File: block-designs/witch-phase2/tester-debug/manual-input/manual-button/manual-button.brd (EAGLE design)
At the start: 27.9 x 27.9 mm, 8 parts

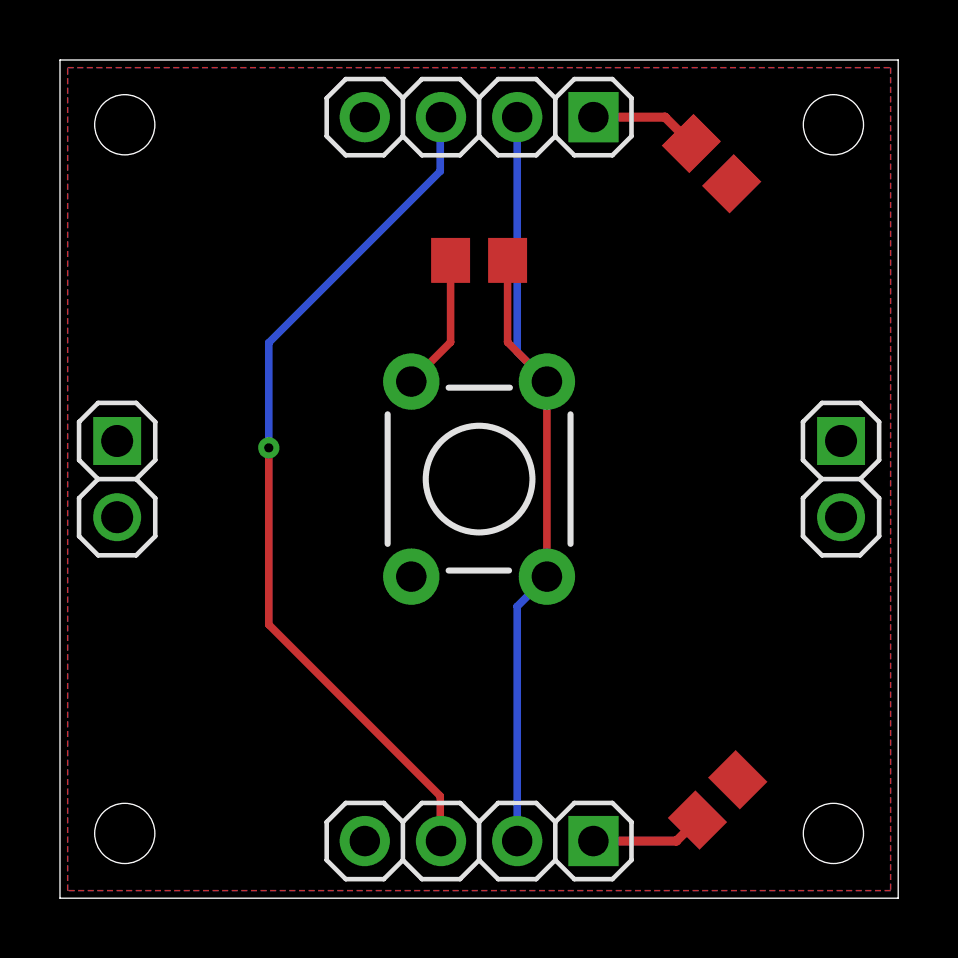
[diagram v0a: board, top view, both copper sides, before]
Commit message: switch to using a schmitt trigger with OR gate for clock output
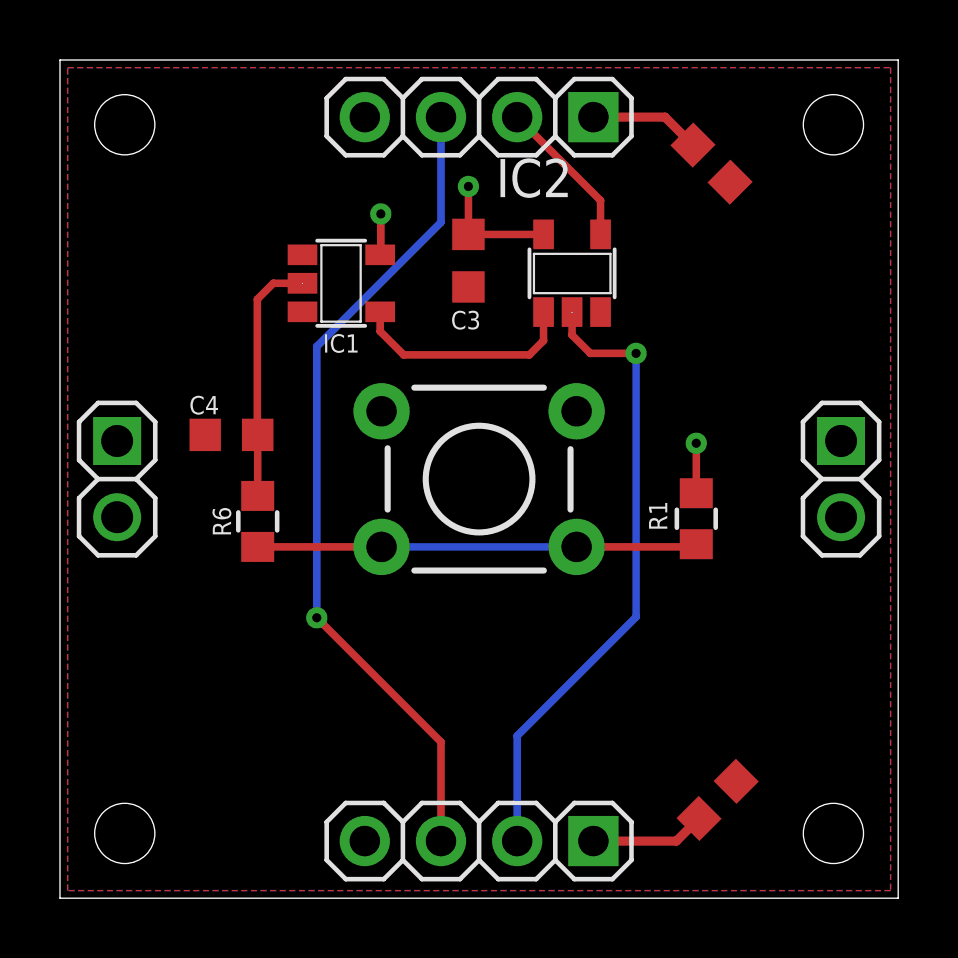
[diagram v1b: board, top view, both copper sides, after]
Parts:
- added C4: 1uF, resistor:C0603K
- added IC1: 74LVC1G14DBV, 74xx-little-us:SOT23-5
- added IC2: 74AHC1G32DBV, 74xx-little-us:SOT23-5
- added R1: 100k, resistor:R0603
- added R6: 10k, resistor:R0603
- C1, C2, C3: device resistor:C0805 -> resistor:C0603K
- moved C3 0.36 mm to (13.6, 21.3), turned to 270 degrees
- turned S1 to 0 degrees
- renumbered S2 to S1
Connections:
- removed net CLOCK: C3.2, JP2.2, JP4.2, S1.1, S1.2
- new net CLOCK_IN: IC2.2, JP4.2
- new net CLOCK_OUT: IC2.4, JP2.2
- new net DA_IN: IC1.4, IC2.1
- new net N$1: R1.1, R6.1, S1.3, S1.4
- new net N$2: C4.1, IC1.2, R6.2
- net GND: now also C3.2, C4.2, IC1.3, IC2.3, S1.1, S1.2
- net VCC: now also IC1.5, IC2.5, R1.2; no longer S1.3, S1.4
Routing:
- net CLOCK: track 29.5 -> 0.00 mm
- net CLOCK_IN: track 0.00 -> 21.1 mm, vias 0 -> 1
- net N$1: track 0.00 -> 14.7 mm
- net N$2: track 0.00 -> 8.28 mm
- net DA_IN: track 0.00 -> 7.58 mm
- net CLOCK_OUT: track 0.00 -> 5.06 mm
- net VCC: track 12.0 -> 14.7 mm, vias 0 -> 3
- net ZC: track 28.8 -> 27.6 mm
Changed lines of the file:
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@@
 </autorouter>
 <elements>
-<element name="C1" library="resistor" package="C0805" value="" x="21.717" y="24.4856" smashed="yes" rot="R315">
+<element name="C1" library="resistor" package="C0603K" value="" x="21.717" y="24.4856" smashed="yes" rot="R315">
 <attribute name="VALUE" x="19.4719375" y="23.49776875" size="1.27" layer="27" rot="R315"/>
 </element>
-<element name="C2" library="resistor" package="C0805" value="" x="21.9202" y="3.2766" smashed="yes" rot="R45">
+<element name="C2" library="resistor" package="C0603K" value="" x="21.9202" y="3.2766" smashed="yes" rot="R45">
 <attribute name="VALUE" x="22.90803125" y="1.031534375" size="1.27" layer="27" rot="R45"/>
 </element>
@@
 <attribute name="VALUE" x="22.86" y="17.78" size="1.27" layer="27" rot="R270"/>
 </element>
-<element name="S2" library="SparkFun-Electromechanical" package="TACTILE-PTH" value="" x="13.97" y="13.97" smashed="yes" rot="R270"/>
-<element name="C3" library="resistor" package="C0805" value="" x="13.97" y="21.2598" smashed="yes">
-<attribute name="VALUE" x="12.7" y="18.7198" size="1.27" layer="27"/>
+<element name="S1" library="SparkFun-Electromechanical" package="TACTILE-PTH" value="" x="13.97" y="13.97" smashed="yes"/>
+<element name="C4" library="resistor" package="C0603K" value="1uF" x="5.715" y="15.4432" smashed="yes" rot="R180">
+<attribute name="NAME" x="5.3086" y="16.7386" size="0.6096" layer="25" rot="R180"/>
+<attribute name="VALUE" x="6.985" y="17.9832" size="1.27" layer="27" rot="R180"/>
 </element>
+<element name="R6" library="resistor" package="R0603" value="10k" x="6.5913" y="12.5603" smashed="yes" rot="R90">
+<attribute name="NAME" x="5.7023" y="12.0523" size="0.6096" layer="25" rot="R90"/>
+<attribute name="VALUE" x="9.1313" y="11.9253" size="1.27" layer="27" rot="R90"/>
+</element>
+<element name="R1" library="resistor" package="R0603" value="100k" x="21.209" y="12.6492" smashed="yes" rot="R90">
+<attribute name="NAME" x="20.2438" y="12.2428" size="0.6096" layer="25" rot="R90"/>
+<attribute name="VALUE" x="23.749" y="12.0142" size="1.27" layer="27" rot="R90"/>
+</element>
+<element name="C3" library="resistor" package="C0603K" value="" x="13.6144" y="21.250909375" smashed="yes" rot="R270">
+<attribute name="NAME" x="13.026490625" y="18.9634" size="0.6096" layer="25"/>
+<attribute name="VALUE" x="11.9644" y="22.050909375" size="1.016" layer="27" rot="R270"/>
+</element>
+<element name="IC1" library="74xx-little-us" package="SOT23-5" value="74LVC1G14DBV" x="9.3726" y="20.4978" smashed="yes" rot="R270">
+<attribute name="NAME" x="8.763" y="18.1864" size="0.6096" layer="25"/>
+<attribute name="VALUE" x="5.5626" y="23.0378" size="1.27" layer="27" rot="R270"/>
+</element>
+<element name="IC2" library="74xx-little-us" package="SOT23-5" value="74AHC1G32DBV" x="17.0688" y="20.828"/>
 </elements>
 <signals>
@@
 <contactref element="JP1" pad="2"/>
 <contactref element="JP3" pad="2"/>
-</signal>
-<signal name="CLOCK">
-<contactref element="JP2" pad="2"/>
-<contactref element="JP4" pad="2"/>
-<contactref element="S2" pad="1"/>
-<contactref element="S2" pad="2"/>
-<wire x1="15.24" y1="26.035" x2="15.24" y2="18.2118" width="0.254" layer="16"/>
-<wire x1="15.24" y1="18.2118" x2="16.2306" y2="17.2212" width="0.254" layer="16"/>
-<wire x1="16.2306" y1="10.7188" x2="15.24" y2="9.7282" width="0.254" layer="16"/>
-<wire x1="15.24" y1="9.7282" x2="15.24" y2="1.905" width="0.254" layer="16"/>
-<wire x1="16.2306" y1="17.2212" x2="16.2306" y2="10.7188" width="0.254" layer="1"/>
+<contactref element="C4" pad="2"/>
+<contactref element="S1" pad="1"/>
+<contactref element="S1" pad="2"/>
 <contactref element="C3" pad="2"/>
-<wire x1="14.92" y1="21.2598" x2="14.92" y2="18.5318" width="0.254" layer="1"/>
-<wire x1="14.92" y1="18.5318" x2="16.2306" y2="17.2212" width="0.254" layer="1"/>
+<contactref element="IC1" pad="3"/>
+<contactref element="IC2" pad="3"/>
 </signal>
 <signal name="ZC">
 <contactref element="JP2" pad="3"/>
 <contactref element="JP4" pad="3"/>
-<via x="6.9596" y="15.0114" extent="1-16" drill="0.3048"/>
-<wire x1="6.9596" y1="15.0114" x2="6.9596" y2="9.1186" width="0.254" layer="1"/>
-<wire x1="6.9596" y1="9.1186" x2="12.6746" y2="3.4036" width="0.254" layer="1"/>
-<wire x1="12.6746" y1="3.4036" x2="12.6746" y2="1.9304" width="0.254" layer="1"/>
-<wire x1="12.6746" y1="1.9304" x2="12.7" y2="1.905" width="0.254" layer="1"/>
-<wire x1="12.6746" y1="26.0096" x2="12.6746" y2="24.2316" width="0.254" layer="16"/>
-<wire x1="12.6746" y1="24.2316" x2="6.9596" y2="18.5166" width="0.254" layer="16"/>
-<wire x1="6.9596" y1="18.5166" x2="6.9596" y2="15.0114" width="0.254" layer="16"/>
-<wire x1="12.6746" y1="26.0096" x2="12.7" y2="26.035" width="0" layer="19" extent="16-16"/>
+<wire x1="12.7" y1="26.035" x2="12.7" y2="22.5298" width="0.254" layer="16"/>
+<via x="8.5598" y="9.3472" extent="1-16" drill="0.3048"/>
+<wire x1="12.7" y1="22.5298" x2="8.5598" y2="18.3896" width="0.254" layer="16"/>
+<wire x1="8.5598" y1="18.3896" x2="8.5598" y2="9.3472" width="0.254" layer="16"/>
+<wire x1="8.5598" y1="9.3472" x2="12.7" y2="5.207" width="0.254" layer="1"/>
+<wire x1="12.7" y1="5.207" x2="12.7" y2="1.905" width="0.254" layer="1"/>
 </signal>
 <signal name="VCC">
@@
 <contactref element="JP2" pad="1"/>
 <contactref element="JP4" pad="1"/>
-<wire x1="21.248446875" y1="2.604846875" x2="20.5486" y2="1.905" width="0.3048" layer="1"/>
+<wire x1="21.30148125" y1="2.65788125" x2="20.5486" y2="1.905" width="0.3048" layer="1"/>
 <wire x1="20.5486" y1="1.905" x2="17.78" y2="1.905" width="0.3048" layer="1"/>
-<wire x1="21.045246875" y1="25.15735" x2="20.167596875" y2="26.035" width="0.3048" layer="1"/>
+<wire x1="21.09828125" y1="25.104315625" x2="20.167596875" y2="26.035" width="0.3048" layer="1"/>
 <wire x1="20.167596875" y1="26.035" x2="17.78" y2="26.035" width="0.3048" layer="1"/>
-<contactref element="S2" pad="4"/>
-<contactref element="S2" pad="3"/>
 <contactref element="JP1" pad="1"/>
 <contactref element="JP3" pad="1"/>
+<contactref element="R1" pad="2"/>
+<wire x1="10.6726" y1="21.4478" x2="10.6934" y2="21.4686" width="0.254" layer="1"/>
+<via x="10.6934" y="22.8092" extent="1-16" drill="0.3048"/>
+<wire x1="16.1188" y1="22.128" x2="16.1036" y2="22.1432" width="0.254" layer="1"/>
+<via x="13.6144" y="23.7236" extent="1-16" drill="0.3048"/>
 <contactref element="C3" pad="1"/>
-<wire x1="13.02" y1="21.2598" x2="13.02" y2="18.5318" width="0.254" layer="1"/>
-<wire x1="13.02" y1="18.5318" x2="11.7094" y2="17.2212" width="0.254" layer="1"/>
+<via x="21.209" y="15.1638" extent="1-16" drill="0.3048"/>
+<wire x1="21.209" y1="13.4992" x2="21.209" y2="15.1638" width="0.254" layer="1"/>
+<wire x1="13.6144" y1="22.125909375" x2="13.6144" y2="23.7236" width="0.254" layer="1"/>
+<contactref element="IC1" pad="5"/>
+<wire x1="10.6934" y1="21.4686" x2="10.6934" y2="22.8092" width="0.254" layer="1"/>
+<contactref element="IC2" pad="5"/>
+<wire x1="16.1188" y1="22.128" x2="16.116709375" y2="22.125909375" width="0.254" layer="1"/>
+<wire x1="16.116709375" y1="22.125909375" x2="13.6144" y2="22.125909375" width="0.254" layer="1"/>
+</signal>
+<signal name="DA_IN">
+<wire x1="11.4554" y1="18.1102" x2="15.6464" y2="18.1102" width="0.254" layer="1"/>
+<wire x1="10.6726" y1="18.893" x2="11.4554" y2="18.1102" width="0.254" layer="1"/>
+<contactref element="IC1" pad="4"/>
+<wire x1="10.6726" y1="18.893" x2="10.6726" y2="19.5478" width="0.254" layer="1"/>
+<contactref element="IC2" pad="1"/>
+<wire x1="15.6464" y1="18.1102" x2="16.1188" y2="18.5826" width="0.254" layer="1"/>
+<wire x1="16.1188" y1="18.5826" x2="16.1188" y2="19.538" width="0.254" layer="1"/>
+</signal>
+<signal name="N$2">
+<contactref element="R6" pad="2"/>
+<contactref element="C4" pad="1"/>
+<wire x1="7.112" y1="20.4978" x2="6.5786" y2="19.9644" width="0.254" layer="1"/>
+<wire x1="6.5786" y1="19.9644" x2="6.5786" y2="15.4546" width="0.254" layer="1"/>
+<wire x1="6.5786" y1="15.4546" x2="6.59" y2="15.4432" width="0.254" layer="1"/>
+<wire x1="6.59" y1="15.4432" x2="6.59" y2="13.4116" width="0.254" layer="1"/>
+<wire x1="6.59" y1="13.4116" x2="6.5913" y2="13.4103" width="0.254" layer="1"/>
+<contactref element="IC1" pad="2"/>
+<wire x1="8.0826" y1="20.4978" x2="7.112" y2="20.4978" width="0.254" layer="1"/>
+</signal>
+<signal name="N$1">
+<contactref element="R6" pad="1"/>
+<contactref element="S1" pad="3"/>
+<contactref element="S1" pad="4"/>
+<contactref element="R1" pad="1"/>
+<wire x1="10.7188" y1="11.7094" x2="17.2212" y2="11.7094" width="0.254" layer="16"/>
+<wire x1="17.2212" y1="11.7094" x2="21.1988" y2="11.7094" width="0.254" layer="1"/>
+<wire x1="21.1988" y1="11.7094" x2="21.209" y2="11.7992" width="0.254" layer="1"/>
+<wire x1="6.5913" y1="11.7103" x2="10.7179" y2="11.7103" width="0.254" layer="1"/>
+<wire x1="10.7179" y1="11.7103" x2="10.7188" y2="11.7094" width="0.254" layer="1"/>
+</signal>
+<signal name="CLOCK_IN">
+<contactref element="JP4" pad="2"/>
+<wire x1="19.2024" y1="9.3726" x2="19.2024" y2="18.161" width="0.254" layer="16"/>
+<via x="19.2024" y="18.161" extent="1-16" drill="0.3048"/>
+<wire x1="19.2024" y1="18.161" x2="17.6784" y2="18.161" width="0.254" layer="1"/>
+<wire x1="17.6784" y1="18.161" x2="17.0688" y2="18.7706" width="0.254" layer="1"/>
+<wire x1="15.24" y1="1.905" x2="15.24" y2="5.4102" width="0.254" layer="16"/>
+<wire x1="15.24" y1="5.4102" x2="19.2024" y2="9.3726" width="0.254" layer="16"/>
+<contactref element="IC2" pad="2"/>
+<wire x1="17.0688" y1="18.7706" x2="17.0688" y2="19.538" width="0.254" layer="1"/>
+</signal>
+<signal name="CLOCK_OUT">
+<contactref element="JP2" pad="2"/>
+<wire x1="18.0188" y1="23.2562" x2="15.24" y2="26.035" width="0.254" layer="1"/>
+<contactref element="IC2" pad="4"/>
+<wire x1="18.0188" y1="22.128" x2="18.0188" y2="23.2562" width="0.254" layer="1"/>
 </signal>
 </signals>
